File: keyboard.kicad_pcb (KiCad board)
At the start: 2 copper layers, 75.4 x 113.7 mm, 131 parts, among them IC1 ATMEGA32U4, J1 MINI-B, M1 HOLE, M10 HOLE, M11 HOLE, M12 HOLE, M13 HOLE, M14 HOLE, M15 HOLE, M16 HOLE, M17 HOLE, M2 HOLE, M3 HOLE, M4 HOLE, M5 HOLE, M6 HOLE, M7 HOLE, M8 HOLE, M9 HOLE, P1 MISO, P10 ROW4, P11 ROW5, P12 ROW6, P13 COL1, P14 COL2, P15 COL3, P16 COL4, P17 FNLED, P18 Vcc, P19 GND, P2 Vcc, P20 SCLM, P200 GND, P201 GND, P202 GND, P203 GND, P204 GND, P205 GND, P21 SDAM, P3 SCK, P4 MOSI, P5 RES, P6 GND, P7 ROW1, P8 ROW2, P9 ROW3, U1 MCP23018, X1 7M-16.000MAAJ-T

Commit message: v0.12.2
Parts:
- J1: value MINI-B -> USB MINI-B
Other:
- board text added: "Rev 0.12.2"
- board text removed: "Rev 0.12.1"

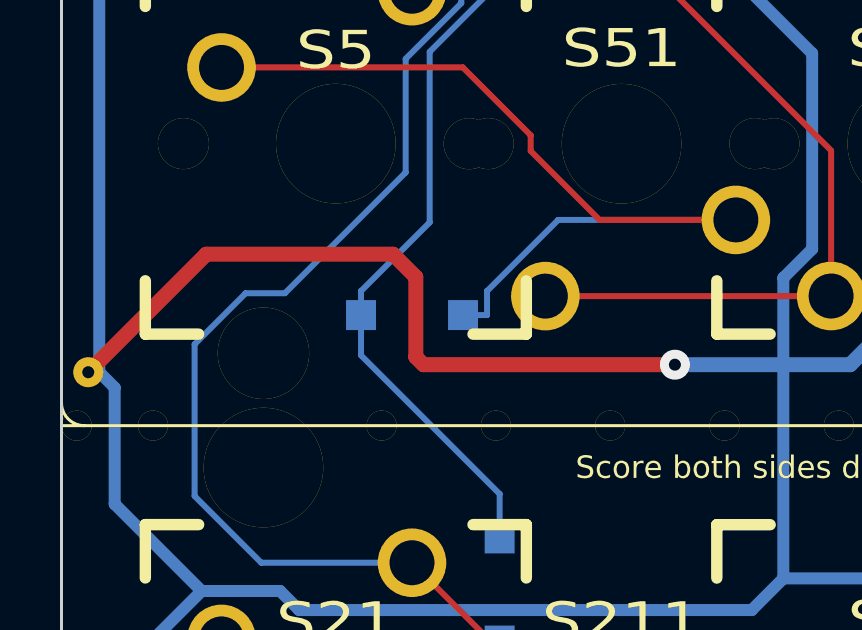
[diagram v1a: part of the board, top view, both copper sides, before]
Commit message: Fixed silkscreen
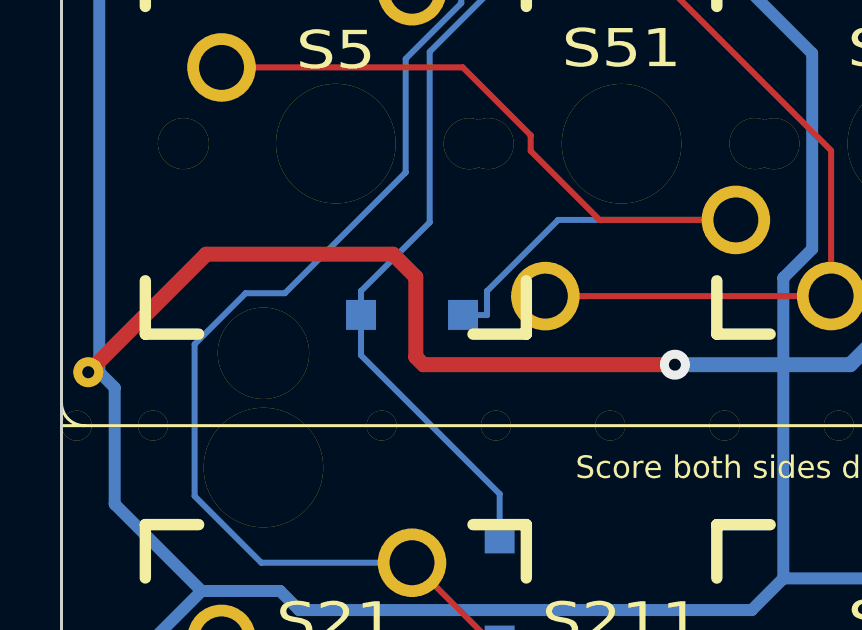
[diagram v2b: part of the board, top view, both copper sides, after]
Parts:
- turned D5 to 0 degrees
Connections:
- D5 pad 1: N-0000064 (its old number) -> /Matrix/col1
- D5 pad 2: /Matrix/col1 -> N-0000063
- S5 pad 2: N-0000064 (its old number) -> N-0000063
- S51 pad 2: N-0000064 (its old number) -> N-0000063
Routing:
- net N-0000064 (its old number): track 30.4 -> 0.00 mm
- net N-0000063: track 0.00 -> 30.4 mm

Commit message: v0.12.3
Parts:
- D1, D10, D11, D12, D13, D14, D15, D16, D17, D18, D19, D2, D20, D21, D22, D23, D24, D3, D4, D5, D6, D7, D8, D9: footprint SOD-123 -> SOD-123(A-C)
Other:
- board text added: "Rev 0.12.3"
- board text removed: "Rev 0.12.2"
